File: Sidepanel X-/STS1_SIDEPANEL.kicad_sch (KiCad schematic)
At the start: 3 parts, among them J1 Conn_02x04_Odd_Even, J2 Conn_02x02_Odd_Even

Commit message: Review Ready for V2.0
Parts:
- J1: value Conn_02x04_Odd_Even -> (none); footprint SamacSys:M808280842 -> (none)
- J2: value Conn_02x02_Odd_Even -> (none); footprint USER_Passiv:M80-8280442 -> (none)
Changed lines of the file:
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@@
     (in_bom yes) (on_board yes) (fields_autoplaced)
     (property "Reference" "J1" (id 0) (at 40.64 60.96 0))
-    (property "Value" "Conn_02x04_Odd_Even" (id 1) (at 40.64 63.5 0))
-    (property "Footprint" "SamacSys:M808280842" (id 2) (at 39.37 69.85 0)
+    (property "Value" "" (id 1) (at 40.64 63.5 0))
+    (property "Footprint" "" (id 2) (at 39.37 69.85 0)
       (effects (font (size 1.27 1.27)) hide)
     )
@@
     (in_bom yes) (on_board yes) (fields_autoplaced)
     (property "Reference" "J2" (id 0) (at 86.36 66.04 0))
-    (property "Value" "Conn_02x02_Odd_Even" (id 1) (at 86.36 68.58 0))
-    (property "Footprint" "USER_Passiv:M80-8280442" (id 2) (at 85.09 72.39 0)
+    (property "Value" "" (id 1) (at 86.36 68.58 0))
+    (property "Footprint" "" (id 2) (at 85.09 72.39 0)
       (effects (font (size 1.27 1.27)) hide)
     )
@@
     )
     (path "/4f87559b-6bba-4ff6-97a7-dad9a308db2d/934b6342-5d8d-49da-bf4f-f7fa77f16f34"
-      (reference "CUR1") (unit 1) (value "TMCS1101A3BQDT") (footprint "SOIC127P600X175-8N")
+      (reference "CUR1") (unit 1) (value "TMCS1101A3BQDT") (footprint "Package_SO:SOIC-8_3.9x4.9mm_P1.27mm")
     )
     (path "/4f87559b-6bba-4ff6-97a7-dad9a308db2d/a554cf31-0806-4740-ba0b-f0d59599f4ca"
@@
     )
     (path "/4f87559b-6bba-4ff6-97a7-dad9a308db2d/c6a198d2-e0e4-4d6d-8a2a-bdeb249501be"
-      (reference "DOUT1") (unit 1) (value "SMM4F5.0") (footprint "SamacSys:STMITE")
+      (reference "DOUT1") (unit 1) (value "SMM4F5.0") (footprint "Diode_SMD:D_0603_1608Metric")
     )
     (path "/9d03bb93-a9aa-424f-bd25-022f173efd1d/d9839939-8918-48f3-b4b2-d753b1d9a645"
-      (reference "IC1") (unit 1) (value "TMP112AQDRLRQ1") (footprint "SamacSys:SOTFL50P160X60-6N")
+      (reference "IC1") (unit 1) (value "TMP112AQDRLRQ1") (footprint "Package_TO_SOT_SMD:SOT-563")
     )
     (path "/7d4ab197-adca-450c-9fc5-7a95ff72b885"
-      (reference "J1") (unit 1) (value "Conn_02x04_Odd_Even") (footprint "SamacSys:M808280842")
+      (reference "J1") (unit 1) (value "Conn_02x04_Odd_Even") (footprint "STS_Connector:M808280842")
     )
     (path "/9272ccd5-e950-4f99-baec-47da7f19129b"
-      (reference "J2") (unit 1) (value "Conn_02x02_Odd_Even") (footprint "USER_Passiv:M80-8280442")
+      (reference "J2") (unit 1) (value "Conn_02x02_Odd_Even") (footprint "STS_Connector:M808280442")
     )
     (path "/4f87559b-6bba-4ff6-97a7-dad9a308db2d/bfe4e68f-4cef-4b31-adff-8df094bc3870"
-      (reference "L_IN1") (unit 1) (value "10u") (footprint "SamacSys:INDPM5650X530N")
+      (reference "L_IN1") (unit 1) (value "10u") (footprint "Inductor_SMD:L_0805_2012Metric")
     )
     (path "/4f87559b-6bba-4ff6-97a7-dad9a308db2d/679b2e27-da22-4f13-a86e-25be83598a10"
-      (reference "MPPT1") (unit 1) (value "SPV1040TTR") (footprint "SamacSys:SOP65P640X120-8N")
+      (reference "MPPT1") (unit 1) (value "SPV1040TTR") (footprint "Package_SO:TSSOP-8_4.4x3mm_P0.65mm")
     )
     (path "/6503b427-07c6-4391-8fa6-4757fb4daa6c"
@@
     )
     (path "/9d03bb93-a9aa-424f-bd25-022f173efd1d/a83d6342-0e16-4131-8bb9-e65e4d72dab0"
-      (reference "U1") (unit 1) (value "GUVA-C32SM") (footprint "USER_Optic:OLGA 2mm x 2,3mm")
-    )
-  )
+      (reference "U1") (unit 1) (value "GUVA-C32SM") (footprint "Package_SO:SO-4_4.4x3.6mm_P2.54mm")
+    )
+  )

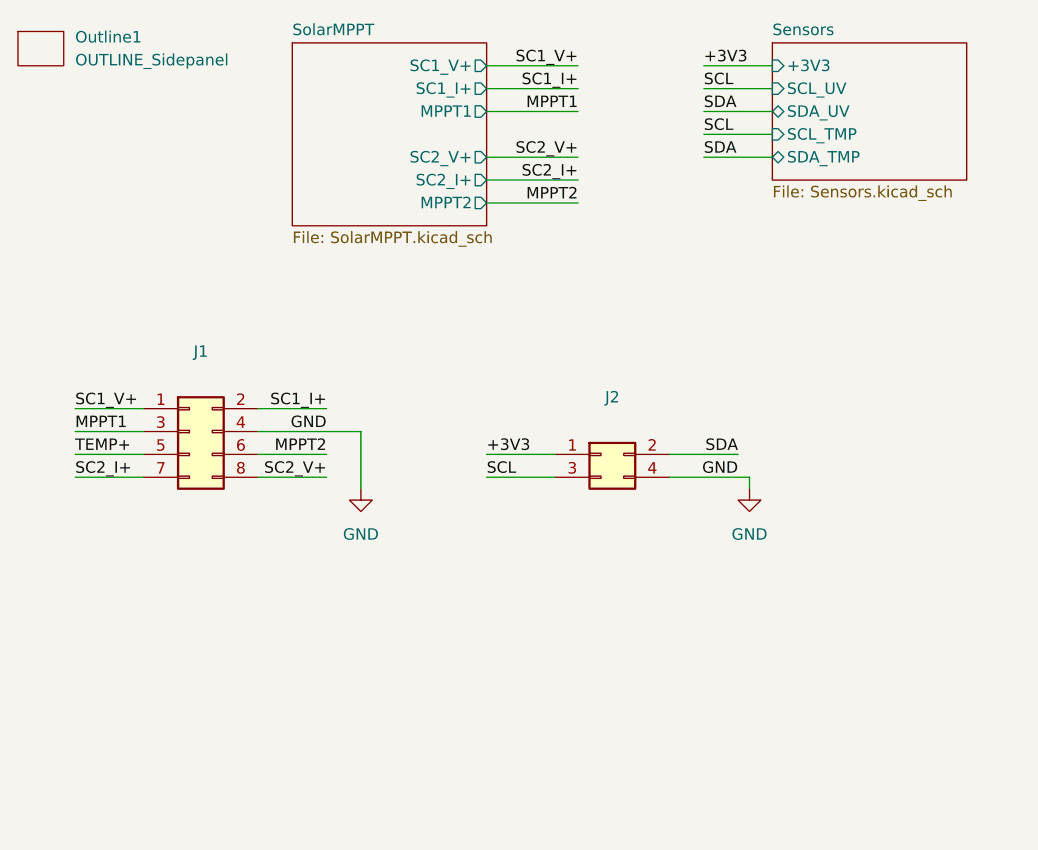
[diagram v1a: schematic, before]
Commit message: Paar Fehler behoben, Z+ no MOSFET
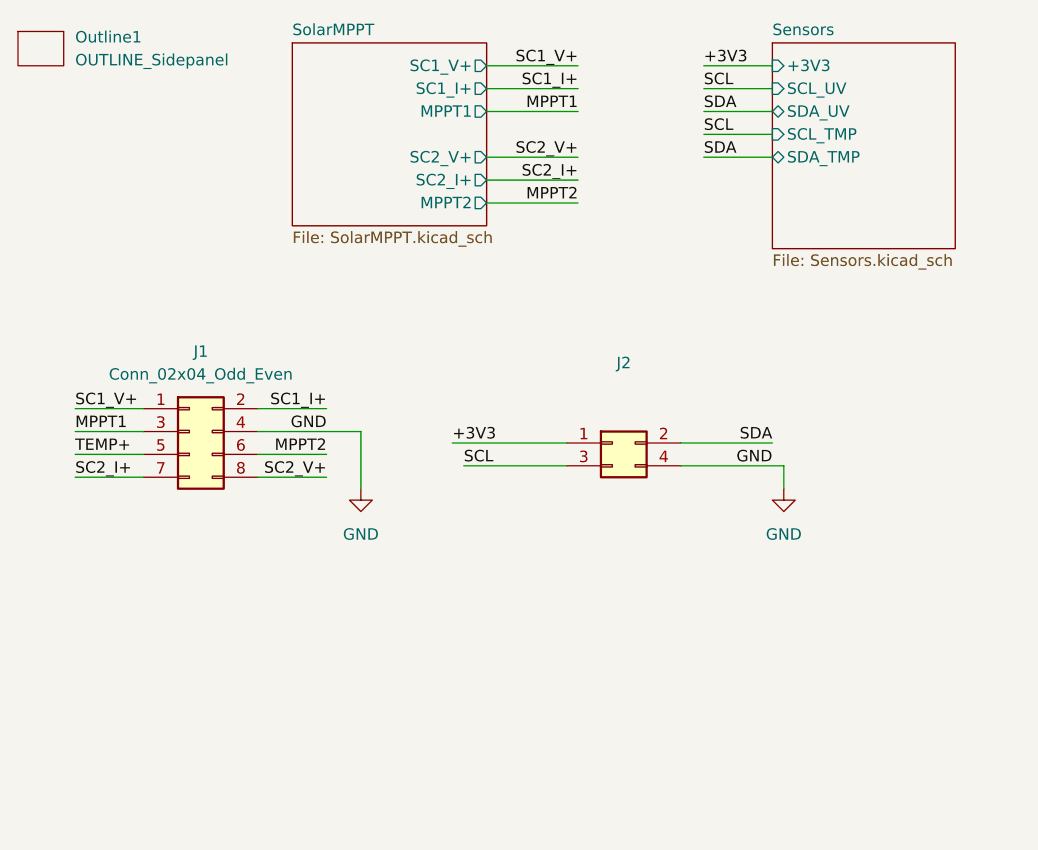
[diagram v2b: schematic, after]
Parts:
- J1: value (none) -> Conn_02x04_Odd_Even; footprint (none) -> STS_Connector:M808280842
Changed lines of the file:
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@@
     (stroke (width 0) (type default) (color 0 0 0 0))
   )
-  (wire (pts (xy 101.6 76.2) (xy 101.6 74.93))
+  (wire (pts (xy 105.41 76.2) (xy 105.41 73.66))
     (stroke (width 0) (type default) (color 0 0 0 0))
   )
@@
     (stroke (width 0) (type default) (color 0 0 0 0))
   )
-  (wire (pts (xy 72.39 72.39) (xy 80.01 72.39))
+  (wire (pts (xy 68.58 71.12) (xy 81.28 71.12))
     (stroke (width 0) (type default) (color 0 0 0 0))
   )
@@
     (stroke (width 0) (type default) (color 0 0 0 0))
   )
-  (wire (pts (xy 92.71 74.93) (xy 101.6 74.93))
+  (wire (pts (xy 93.98 73.66) (xy 105.41 73.66))
     (stroke (width 0) (type default) (color 0 0 0 0))
   )
@@
     (stroke (width 0) (type default) (color 0 0 0 0))
   )
-  (wire (pts (xy 72.39 74.93) (xy 80.01 74.93))
+  (wire (pts (xy 69.85 73.66) (xy 81.28 73.66))
     (stroke (width 0) (type default) (color 0 0 0 0))
   )
@@
     (stroke (width 0) (type default) (color 0 0 0 0))
   )
-  (wire (pts (xy 92.71 72.39) (xy 100.33 72.39))
+  (wire (pts (xy 93.98 71.12) (xy 104.14 71.12))
     (stroke (width 0) (type default) (color 0 0 0 0))
   )
@@
     (effects (font (size 1.27 1.27)) (justify right bottom))
   )
-  (label "SCL" (at 72.39 74.93 0)
-    (effects (font (size 1.27 1.27)) (justify left bottom))
-  )
-  (label "GND" (at 100.33 74.93 180)
+  (label "SCL" (at 69.85 73.66 0)
+    (effects (font (size 1.27 1.27)) (justify left bottom))
+  )
+  (label "GND" (at 104.14 73.66 180)
     (effects (font (size 1.27 1.27)) (justify right bottom))
   )
@@
     (effects (font (size 1.27 1.27)) (justify left bottom))
   )
-  (label "+3V3" (at 72.39 72.39 0)
+  (label "+3V3" (at 68.58 71.12 0)
     (effects (font (size 1.27 1.27)) (justify left bottom))
   )
@@
     (effects (font (size 1.27 1.27)) (justify left bottom))
   )
-  (label "SDA" (at 100.33 72.39 180)
+  (label "SDA" (at 104.14 71.12 180)
     (effects (font (size 1.27 1.27)) (justify right bottom))
   )
   (label "SC2_I+" (at 82.55 41.91 180)
     (effects (font (size 1.27 1.27)) (justify right bottom))
+  )
+  (symbol (lib_id "Connector_Generic:Conn_02x02_Odd_Even") (at 86.36 71.12 0) (unit 1)
+    (in_bom yes) (on_board yes) (fields_autoplaced)
+    (property "Reference" "J2" (id 0) (at 87.63 62.23 0))
+    (property "Value" "" (id 1) (at 87.63 64.77 0))
+    (property "Footprint" "" (id 2) (at 86.36 71.12 0)
+      (effects (font (size 1.27 1.27)) hide)
+    )
+    (property "Datasheet" "~" (id 3) (at 86.36 71.12 0)
+      (effects (font (size 1.27 1.27)) hide)
+    )
+    (pin "1")
+    (pin "2")
+    (pin "3")
+    (pin "4")
   )
   (symbol (lib_id "power:GND") (at 58.42 76.2 0) (unit 1)
@@
     (in_bom yes) (on_board yes) (fields_autoplaced)
     (property "Reference" "J1" (id 0) (at 40.64 60.96 0))
-    (property "Value" "" (id 1) (at 40.64 63.5 0))
-    (property "Footprint" "" (id 2) (at 39.37 69.85 0)
+    (property "Value" "Conn_02x04_Odd_Even" (id 1) (at 40.64 63.5 0))
+    (property "Footprint" "STS_Connector:M808280842" (id 2) (at 39.37 69.85 0)
       (effects (font (size 1.27 1.27)) hide)
     )
@@
     (pin "8")
   )
-  (symbol (lib_id "Connector_Generic:Conn_02x02_Odd_Even") (at 85.09 72.39 0) (unit 1)
+  (symbol (lib_id "power:GND") (at 105.41 76.2 0) (unit 1)
     (in_bom yes) (on_board yes) (fields_autoplaced)
-    (property "Reference" "J2" (id 0) (at 86.36 66.04 0))
-    (property "Value" "" (id 1) (at 86.36 68.58 0))
-    (property "Footprint" "" (id 2) (at 85.09 72.39 0)
-      (effects (font (size 1.27 1.27)) hide)
-    )
-    (property "Datasheet" "~" (id 3) (at 85.09 72.39 0)
-      (effects (font (size 1.27 1.27)) hide)
-    )
-    (pin "1")
-    (pin "2")
-    (pin "3")
-    (pin "4")
-  )
-  (symbol (lib_id "power:GND") (at 101.6 76.2 0) (unit 1)
-    (in_bom yes) (on_board yes) (fields_autoplaced)
-    (property "Reference" "#PWR0112" (id 0) (at 101.6 82.55 0)
-      (effects (font (size 1.27 1.27)) hide)
-    )
-    (property "Value" "GND" (id 1) (at 101.6 81.28 0))
-    (property "Footprint" "" (id 2) (at 101.6 76.2 0)
-      (effects (font (size 1.27 1.27)) hide)
-    )
-    (property "Datasheet" "" (id 3) (at 101.6 76.2 0)
+    (property "Reference" "#PWR0112" (id 0) (at 105.41 82.55 0)
+      (effects (font (size 1.27 1.27)) hide)
+    )
+    (property "Value" "GND" (id 1) (at 105.41 81.28 0))
+    (property "Footprint" "" (id 2) (at 105.41 76.2 0)
+      (effects (font (size 1.27 1.27)) hide)
+    )
+    (property "Datasheet" "" (id 3) (at 105.41 76.2 0)
       (effects (font (size 1.27 1.27)) hide)
     )
@@
     )
   )
-  (sheet (at 104.14 26.67) (size 21.59 15.24) (fields_autoplaced)
+  (sheet (at 104.14 26.67) (size 20.32 22.86) (fields_autoplaced)
     (stroke (width 0.1524) (type solid) (color 0 0 0 0))
     (fill (color 0 0 0 0.0000))
@@
       (effects (font (size 1.27 1.27)) (justify left bottom))
     )
-    (property "Sheet file" "Sensors.kicad_sch" (id 1) (at 104.14 42.4946 0)
+    (property "Sheet file" "Sensors.kicad_sch" (id 1) (at 104.14 50.1146 0)
       (effects (font (size 1.27 1.27)) (justify left top))
     )
@@
       (reference "J1") (unit 1) (value "Conn_02x04_Odd_Even") (footprint "STS_Connector:M808280842")
     )
-    (path "/9272ccd5-e950-4f99-baec-47da7f19129b"
+    (path "/459b036d-0fde-43a8-9bcf-7e2c885957e8"
       (reference "J2") (unit 1) (value "Conn_02x02_Odd_Even") (footprint "STS_Connector:M808280442")
     )

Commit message: Next fix
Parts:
- added TH1: Thermistor_NTC, Resistor_SMD:R_0805_2012Metric_Pad1.20x1.40mm_HandSolder, symbol Device:Thermistor_NTC
- J2: value (none) -> Conn_02x02_Odd_Even; footprint (none) -> STS_Connector:M808280442
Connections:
- net GND: now also TH1.2
- net TEMP+: now also TH1.1
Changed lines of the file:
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@@
+    (stroke (width 0) (type default) (color 0 0 0 0))
+  )
+  (wire (pts (xy 33.02 93.345) (xy 40.005 93.345))
     (stroke (width 0) (type default) (color 0 0 0 0))
   )
@@
     (stroke (width 0) (type default) (color 0 0 0 0))
   )
+  (wire (pts (xy 33.02 104.775) (xy 33.02 107.95))
+    (stroke (width 0) (type default) (color 0 0 0 0))
+  )
   (wire (pts (xy 93.98 71.12) (xy 104.14 71.12))
     (stroke (width 0) (type default) (color 0 0 0 0))
@@
     (stroke (width 0) (type default) (color 0 0 0 0))
   )
+  (wire (pts (xy 33.02 93.345) (xy 33.02 97.155))
+    (stroke (width 0) (type default) (color 0 0 0 0))
+  )
   (wire (pts (xy 46.99 69.85) (xy 58.42 69.85))
     (stroke (width 0) (type default) (color 0 0 0 0))
@@
     (effects (font (size 1.27 1.27)) (justify right bottom))
   )
+  (label "TEMP+" (at 40.005 93.345 180)
+    (effects (font (size 1.27 1.27)) (justify right bottom))
+  )
   (label "MPPT2" (at 82.55 44.45 180)
     (effects (font (size 1.27 1.27)) (justify right bottom))
@@
     (in_bom yes) (on_board yes) (fields_autoplaced)
     (property "Reference" "J2" (id 0) (at 87.63 62.23 0))
-    (property "Value" "" (id 1) (at 87.63 64.77 0))
-    (property "Footprint" "" (id 2) (at 86.36 71.12 0)
+    (property "Value" "Conn_02x02_Odd_Even" (id 1) (at 87.63 64.77 0))
+    (property "Footprint" "STS_Connector:M808280442" (id 2) (at 86.36 71.12 0)
       (effects (font (size 1.27 1.27)) hide)
     )
@@
     (pin "8")
   )
+  (symbol (lib_id "Device:Thermistor_NTC") (at 33.02 100.965 0) (unit 1)
+    (in_bom yes) (on_board yes) (fields_autoplaced)
+    (property "Reference" "TH1" (id 0) (at 35.56 100.0124 0)
+      (effects (font (size 1.27 1.27)) (justify left))
+    )
+    (property "Value" "Thermistor_NTC" (id 1) (at 35.56 102.5524 0)
+      (effects (font (size 1.27 1.27)) (justify left))
+    )
+    (property "Footprint" "Resistor_SMD:R_0805_2012Metric_Pad1.20x1.40mm_HandSolder" (id 2) (at 33.02 99.695 0)
+      (effects (font (size 1.27 1.27)) hide)
+    )
+    (property "Datasheet" "~" (id 3) (at 33.02 99.695 0)
+      (effects (font (size 1.27 1.27)) hide)
+    )
+    (pin "1")
+    (pin "2")
+  )
   (symbol (lib_id "power:GND") (at 105.41 76.2 0) (unit 1)
     (in_bom yes) (on_board yes) (fields_autoplaced)
@@
     )
     (property "Datasheet" "" (id 3) (at 105.41 76.2 0)
+      (effects (font (size 1.27 1.27)) hide)
+    )
+    (pin "1")
+  )
+  (symbol (lib_id "power:GND") (at 33.02 107.95 0) (unit 1)
+    (in_bom yes) (on_board yes) (fields_autoplaced)
+    (property "Reference" "#PWR0107" (id 0) (at 33.02 114.3 0)
+      (effects (font (size 1.27 1.27)) hide)
+    )
+    (property "Value" "GND" (id 1) (at 33.02 113.03 0))
+    (property "Footprint" "" (id 2) (at 33.02 107.95 0)
+      (effects (font (size 1.27 1.27)) hide)
+    )
+    (property "Datasheet" "" (id 3) (at 33.02 107.95 0)
       (effects (font (size 1.27 1.27)) hide)
     )
@@
       (reference "#PWR0106") (unit 1) (value "GND") (footprint "")
     )
+    (path "/f525da21-1385-4ff3-a214-599922e911b7"
+      (reference "#PWR0107") (unit 1) (value "GND") (footprint "")
+    )
     (path "/4f87559b-6bba-4ff6-97a7-dad9a308db2d/5bbe5da1-3bad-4b6d-b046-d5fbf4c349d2"
       (reference "#PWR0108") (unit 1) (value "GND") (footprint "")
@@
     )
     (path "/4f87559b-6bba-4ff6-97a7-dad9a308db2d/e7b54c2f-482e-4a97-841f-62a80e0193a8"
-      (reference "SC1") (unit 1) (value "Solar_Cell") (footprint "USER_Activ:3G30A_40x80")
+      (reference "SC1") (unit 1) (value "Solar_Cell") (footprint "STS_Solarcells:3G30A_40x80")
+    )
+    (path "/c33f846f-6e6c-4c0f-948a-22eab21412d5"
+      (reference "TH1") (unit 1) (value "Thermistor_NTC") (footprint "Resistor_SMD:R_0805_2012Metric_Pad1.20x1.40mm_HandSolder")
     )
     (path "/9d03bb93-a9aa-424f-bd25-022f173efd1d/a83d6342-0e16-4131-8bb9-e65e4d72dab0"

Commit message: release_2.0, Ordered PCBs
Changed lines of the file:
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@@
     )
     (path "/4f87559b-6bba-4ff6-97a7-dad9a308db2d/c6a198d2-e0e4-4d6d-8a2a-bdeb249501be"
-      (reference "DOUT1") (unit 1) (value "SMM4F5.0") (footprint "Diode_SMD:D_0603_1608Metric")
+      (reference "DOUT1") (unit 1) (value "SMM4F5.0") (footprint "SamacSys:STMITE")
     )
     (path "/9d03bb93-a9aa-424f-bd25-022f173efd1d/d9839939-8918-48f3-b4b2-d753b1d9a645"
@@
     )
     (path "/4f87559b-6bba-4ff6-97a7-dad9a308db2d/bfe4e68f-4cef-4b31-adff-8df094bc3870"
-      (reference "L_IN1") (unit 1) (value "10u") (footprint "Inductor_SMD:L_0805_2012Metric")
+      (reference "L_IN1") (unit 1) (value "10u") (footprint "STS_Inductor_SMD:XAL6060103MEC")
     )
     (path "/4f87559b-6bba-4ff6-97a7-dad9a308db2d/679b2e27-da22-4f13-a86e-25be83598a10"

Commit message: Fixed some DRC errors.
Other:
- sheet SolarMPPT ports: added none; removed MPPT2, SC2_I+, SC2_V+
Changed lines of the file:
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@@
-    (stroke (width 0) (type default) (color 0 0 0 0))
-  )
-  (wire (pts (xy 72.39 39.37) (xy 82.55 39.37))
     (stroke (width 0) (type default) (color 0 0 0 0))
   )
@@
     (stroke (width 0) (type default) (color 0 0 0 0))
   )
-  (wire (pts (xy 72.39 44.45) (xy 82.55 44.45))
-    (stroke (width 0) (type default) (color 0 0 0 0))
-  )
   (wire (pts (xy 96.52 34.29) (xy 104.14 34.29))
     (stroke (width 0) (type default) (color 0 0 0 0))
@@
     (stroke (width 0) (type default) (color 0 0 0 0))
   )
-  (wire (pts (xy 72.39 41.91) (xy 82.55 41.91))
-    (stroke (width 0) (type default) (color 0 0 0 0))
-  )
   (wire (pts (xy 33.02 93.345) (xy 33.02 97.155))
     (stroke (width 0) (type default) (color 0 0 0 0))
@@
     (effects (font (size 1.27 1.27)) (justify right bottom))
   )
-  (label "MPPT2" (at 82.55 44.45 180)
-    (effects (font (size 1.27 1.27)) (justify right bottom))
-  )
   (label "MPPT1" (at 26.67 69.85 0)
     (effects (font (size 1.27 1.27)) (justify left bottom))
@@
     (effects (font (size 1.27 1.27)) (justify right bottom))
   )
-  (label "SC2_V+" (at 82.55 39.37 180)
-    (effects (font (size 1.27 1.27)) (justify right bottom))
-  )
   (label "SC2_V+" (at 54.61 74.93 180)
     (effects (font (size 1.27 1.27)) (justify right bottom))
@@
   )
   (label "SDA" (at 104.14 71.12 180)
-    (effects (font (size 1.27 1.27)) (justify right bottom))
-  )
-  (label "SC2_I+" (at 82.55 41.91 180)
     (effects (font (size 1.27 1.27)) (justify right bottom))
   )
@@
       (effects (font (size 1.27 1.27)) (justify left top))
     )
-    (pin "SC2_I+" output (at 72.39 41.91 0)
-      (effects (font (size 1.27 1.27)) (justify right))
-    )
-    (pin "MPPT2" output (at 72.39 44.45 0)
-      (effects (font (size 1.27 1.27)) (justify right))
-    )
     (pin "SC1_V+" output (at 72.39 29.21 0)
       (effects (font (size 1.27 1.27)) (justify right))
@@
       (effects (font (size 1.27 1.27)) (justify right))
     )
-    (pin "SC2_V+" output (at 72.39 39.37 0)
-      (effects (font (size 1.27 1.27)) (justify right))
-    )
